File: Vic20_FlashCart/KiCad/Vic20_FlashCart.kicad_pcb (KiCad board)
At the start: 2 copper layers, 94.9 x 50 mm, 45 parts, among them J3 Pin Headers, U1 SST39LF040, U2 SST39LF040, U3 IS62C256AL, U4 SN74HCT00PWR, U5 CD74HCT21M96, X1 Cart Fingers

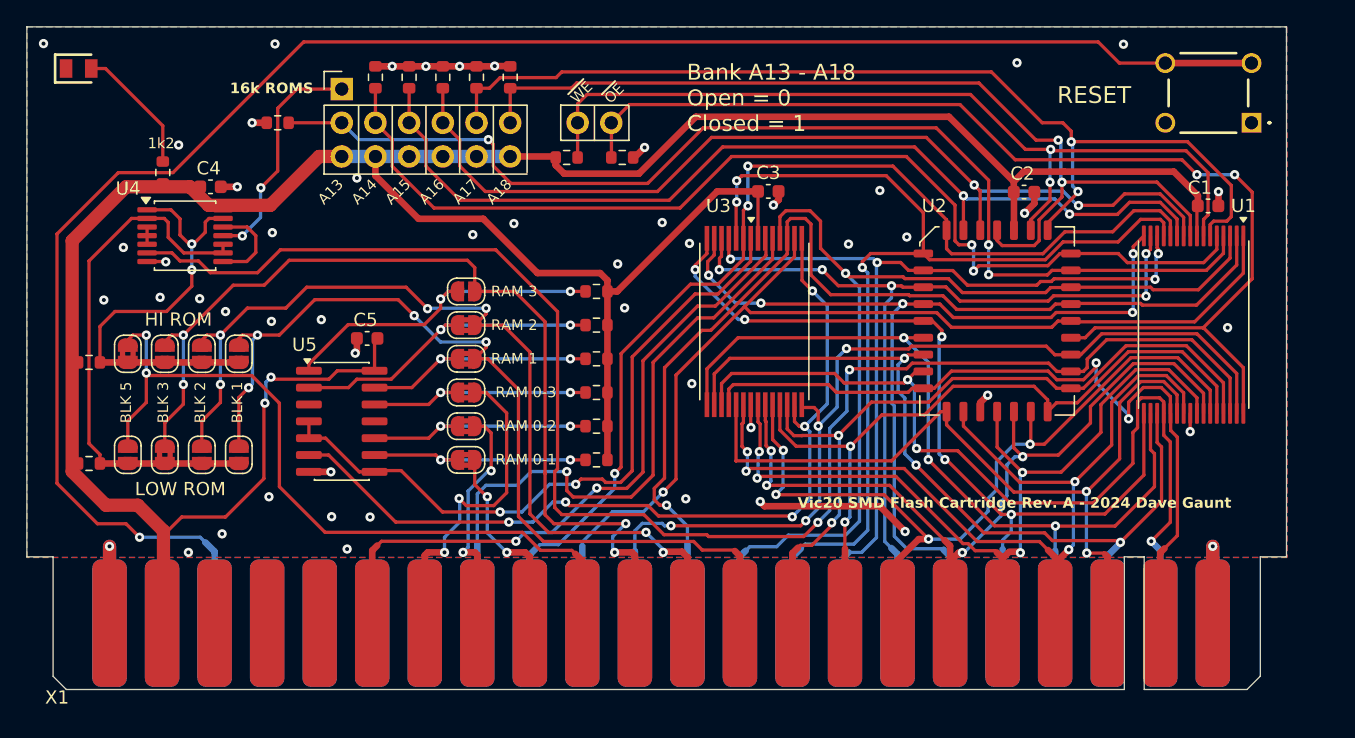
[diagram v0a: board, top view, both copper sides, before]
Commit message: - Updated To KiCad 10.0
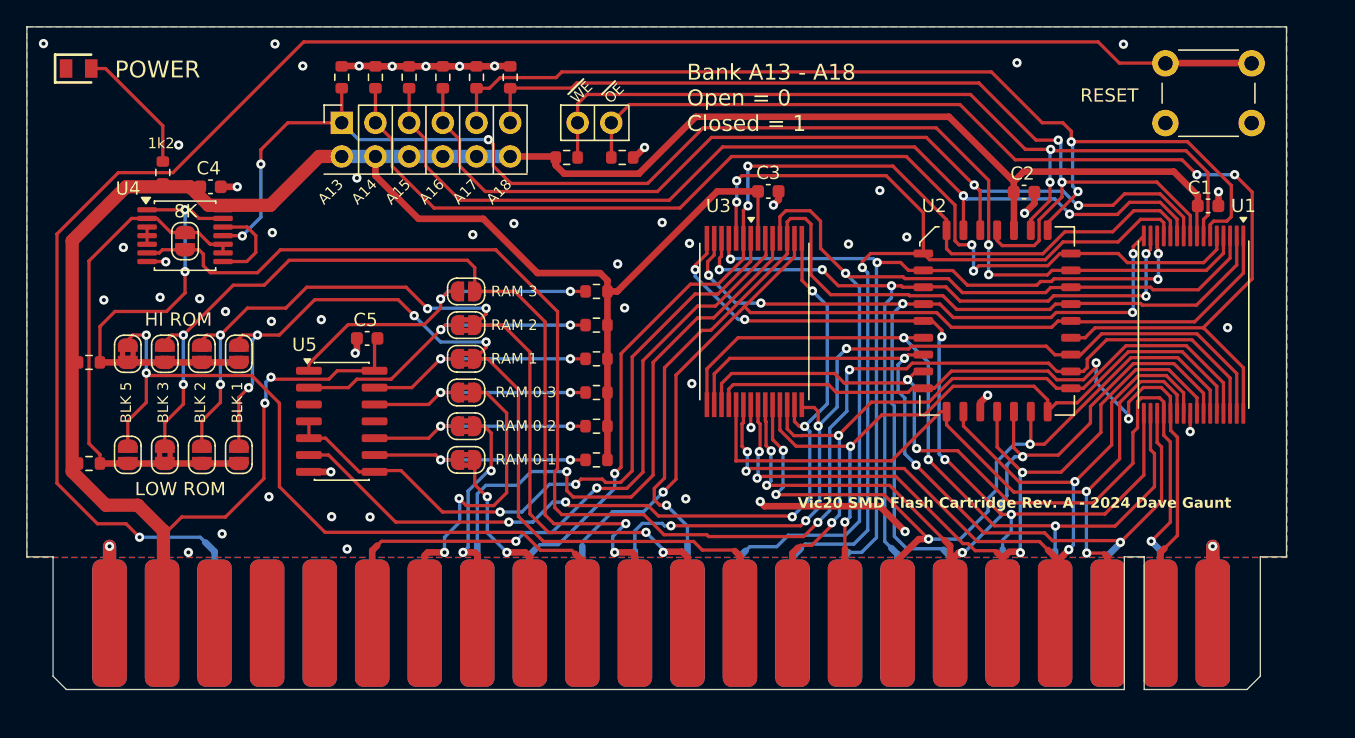
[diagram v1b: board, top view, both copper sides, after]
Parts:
- added JP16: 8K, Jumper:SolderJumper-2_P1.3mm_Open_RoundedPad1.0x1.5mm, F.Cu at (99.9, 90.2)
- J3: footprint Dave Footprints:PinHeader_Vic20_Cartridge -> _Custom:PinHeader_Vic20_Cartridge
- S1: footprint SamacSys_Parts:B3F1052G -> Button_Switch_THT:SW_PUSH_6mm_H4.3mm
- X1: footprint Dave Footprints:VIC20-Cart-Num -> _Custom:VIC20-Cart-Num
- moved S1 7.89 mm to (173.8, 76.8)
- moved R7 5.92 mm to (111.8, 77.9), turned to 90 degrees
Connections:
- net /~{CE} renamed /~{CHIP_ENABLE}
- J3 pad 1: /HI / LO BANK -> /B13
- J3 pad 10: /B17 -> +5V
- J3 pad 11: +5V -> /B18
- J3 pad 12: /B18 -> +5V
- J3 pad 13: +5V -> /~{WRITE_ENABLE}
- J3 pad 14: Net-(J3-~{WE}) -> /~{OUTPUT_ENABLE}
- J3 pad 2: /B13 -> +5V
- J3 pad 3: +5V -> /B14
- J3 pad 4: /B14 -> +5V
- J3 pad 5: +5V -> /B15
- J3 pad 6: /B15 -> +5V
- J3 pad 7: +5V -> /B16
- J3 pad 8: /B16 -> +5V
- J3 pad 9: +5V -> /B17
- R15 pad 2: Net-(J3-~{WE}) -> /~{WRITE_ENABLE}
- R16 pad 1: Net-(J3-~{OE}) -> /~{OUTPUT_ENABLE}
- S1 pad 1: GND -> Net-(X1-~{RESET})
- U1 pad 32: Net-(J3-~{OE}) -> /~{OUTPUT_ENABLE}
- U1 pad 7: Net-(J3-~{WE}) -> /~{WRITE_ENABLE}
- U2 pad 24: Net-(J3-~{OE}) -> /~{OUTPUT_ENABLE}
- U2 pad 31: Net-(J3-~{WE}) -> /~{WRITE_ENABLE}
- U4 pad 11: /HI / LO BANK -> /B13
- U5 pad 11: (no net) -> unconnected-(U5C-NC-Pad11)
- U5 pad 3: (no net) -> unconnected-(U5C-NC-Pad3)
- X1 pad X: Net-(S1-NO_1) -> Net-(X1-~{RESET})
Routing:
- net Net-(X1-~{RESET}): track 0.00 -> 134.9 mm, vias 0 -> 1
- net Net-(S1-NO_1): track 134.9 -> 0.00 mm, vias 1 -> 0
- net Net-(J3-~{OE}): track 84.0 -> 0.00 mm, vias 2 -> 0
- net /~{OUTPUT_ENABLE}: track 0.00 -> 84.0 mm, vias 0 -> 2
- net Net-(J3-~{WE}): track 65.9 -> 0.00 mm, vias 2 -> 0
- net /~{WRITE_ENABLE}: track 0.00 -> 65.9 mm, vias 0 -> 2
- net /HI / LO BANK: track 17.6 -> 0.00 mm, vias 2 -> 0
- net /B13: track 85.8 -> 99.9 mm, vias 3 -> 5
- net GND: track 61.4 -> 62.9 mm, vias 52 -> 53
- net /Block_Low: track 39.9 -> 39.0 mm
- net /~{CHIP_ENABLE}: track 117.1 -> 117.8 mm
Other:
- board text removed: "16k ROMS"
- board text removed: "VIC-20 Dual Serial Cart Mk I Rev B"
